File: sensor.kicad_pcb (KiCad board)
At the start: 2 copper layers, 50 x 50 mm, 34 parts, among them J1 CTRL, J2 EXT_SHUNT, J3 DC_IN, J4 DC_OUT, U1 PCA9615, U2 INA219BIDR

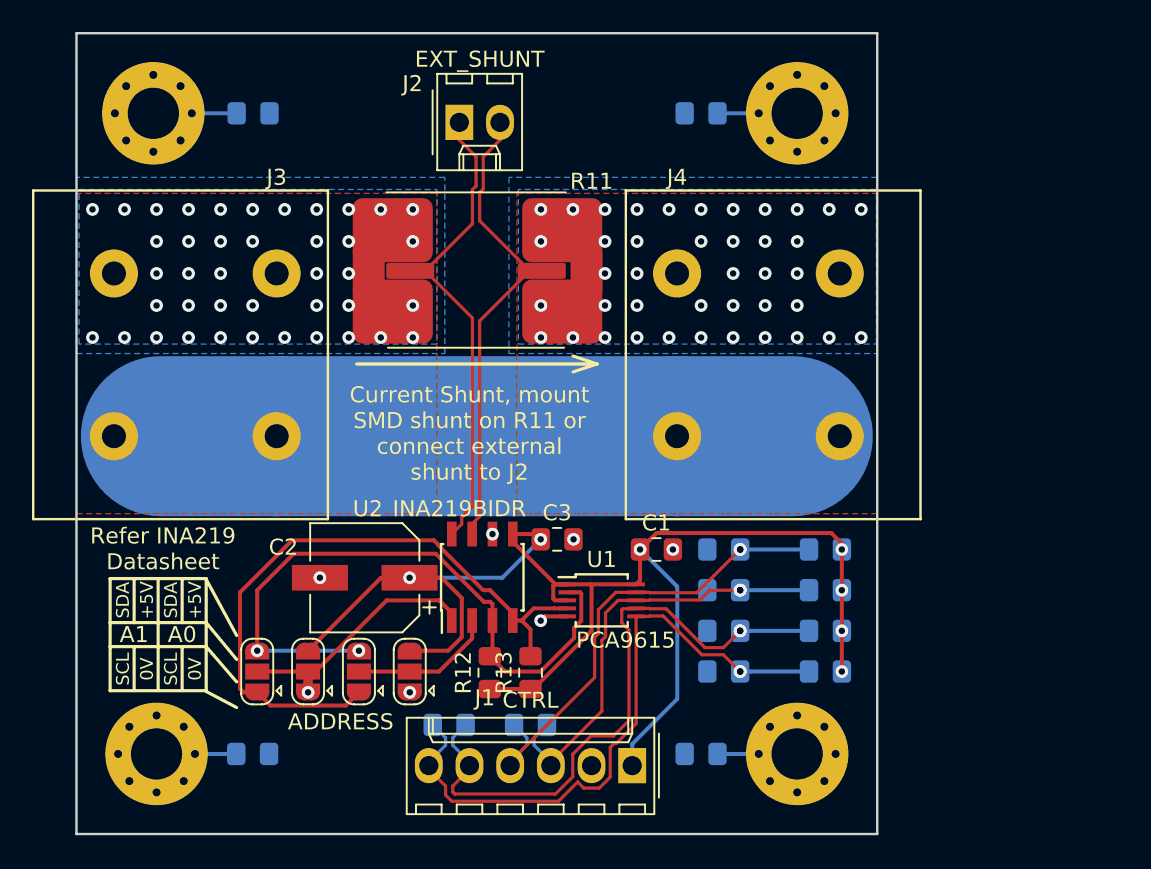
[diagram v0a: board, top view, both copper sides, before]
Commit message: pcb, sch: Drop screw terminals, current shunt.
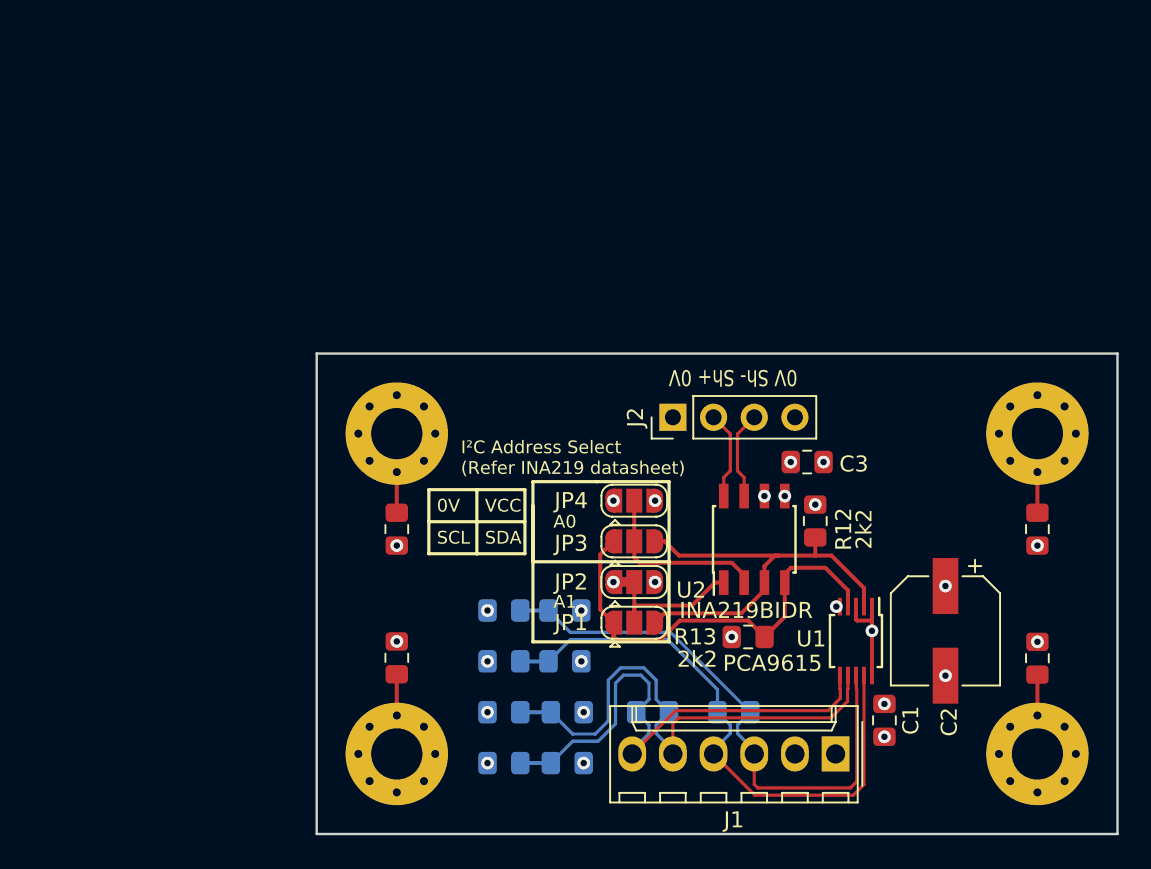
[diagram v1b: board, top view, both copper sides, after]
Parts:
- removed J3: DC_IN, combicon:Phoenix_COMBICON_1706785
- removed J4: DC_OUT, combicon:Phoenix_COMBICON_1706785
- removed R11: R_Shunt, currentshunt:currentshunt
- C4, C5, C6, C7: moved to F.Cu
- J2: value EXT_SHUNT -> Conn_01x04; footprint Connector_Molex:Molex_KK-254_AE-6410-02A_1x02_P2.54mm_Vertical -> Connector_PinHeader_2.54mm:PinHeader_1x04_P2.54mm_Vertical
- moved MH1 68.2 mm to (165.0, 115.0)
- moved C4 59.6 mm to (165.0, 109.0), turned to 90 degrees
- moved C2 36.4 mm to (159.3, 107.3), turned to 270 degrees
- moved C5 33.4 mm to (165.0, 101.0), turned to 270 degrees
- moved MH2 25.0 mm to (165.0, 95.0)
- moved MH3 25.0 mm to (125.0, 95.0)
- moved MH4 25.0 mm to (125.0, 115.0)
- moved JP1 23.7 mm to (139.8, 106.8), turned to 0 degrees
- moved J2 22.7 mm to (142.2, 94.0), turned to 90 degrees
- moved R12 22.4 mm to (151.1, 100.5), turned to 270 degrees
- moved JP2 21.1 mm to (139.8, 104.3), turned to 0 degrees
- moved C7 19.9 mm to (125.0, 109.0), turned to 90 degrees
- moved JP3 19.0 mm to (139.8, 101.7), turned to 0 degrees
- moved C1 17.8 mm to (155.4, 112.9), turned to 270 degrees
- moved R4 17.7 mm to (135.5, 109.2)
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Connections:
- J2 pad 1: /SHUNT+ -> GND
- J2 pad 2: /SHUNT- -> /SHUNT+
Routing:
- net VCC: track 91.0 -> 6.16 mm, vias 7 -> 13
- net GND: track 43.7 -> 0.23 mm, vias 7 -> 15
- net /SHUNT+: track 31.1 -> 5.52 mm
- net /SHUNT-: track 30.5 -> 5.52 mm
- net /SDA: track 41.3 -> 26.9 mm, vias 2 -> 0
- net /SCL: track 41.1 -> 27.2 mm
- net /SDA+: track 27.5 -> 35.6 mm, vias 2 -> 0
- net /SCL-: track 40.0 -> 33.4 mm, vias 2 -> 0
- net /SDA-: track 30.0 -> 36.5 mm, vias 2 -> 0
- net /SCL+: track 39.4 -> 33.3 mm, vias 2 -> 0
- net /A1: track 14.8 -> 9.75 mm
- net Net-(C6-Pad1): track 2.57 -> 4.94 mm
- net /A0: track 9.04 -> 11.3 mm
- net /OUT: vias 41 -> 0
- net /IN: vias 41 -> 0
- added copper zone on In2.Cu, net GND
- added copper zone on In1.Cu, net VCC
- removed copper zone on B.Cu, net /IN
- removed copper zone on F.Cu, net /IN
- removed copper zone on B.Cu, net /OUT
- removed copper zone on F.Cu, net /OUT
- removed copper zone on B.Cu, net GND
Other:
- board size 50 x 50 mm -> 50 x 30 mm
- copper layers 2 -> 4
- board text added: "+SCL-"
- board text added: "+SDA-"
- board text added: "0V Sh- Sh+ 0V"
- board text added: "INA219 Voltage/Current Sensor © 2018 Stuart Longland https://hackaday.io/project/161502"
- board text added: "I²C Address Select (Refer INA219 datasheet)"
- board text added: "Termination"
- board text added: "VCC"
- board text added: "VCC 0V"
- board text removed: "+5V"
- board text removed: "+5V 0V SDA+ SDA- SCL+ SCL-"
- board text removed: "ADDRESS"
- board text removed: "Current Shunt, mount SMD shunt on R11 or connect external shunt to J2"
- board text removed: "Refer INA219 Datasheet"
- board text removed: "Voltage/Current Sensor Board (INA219 + PCA9615) © Stuart Longland https://hackaday.io/project/161502"
